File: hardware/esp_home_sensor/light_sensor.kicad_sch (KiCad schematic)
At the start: 3 parts

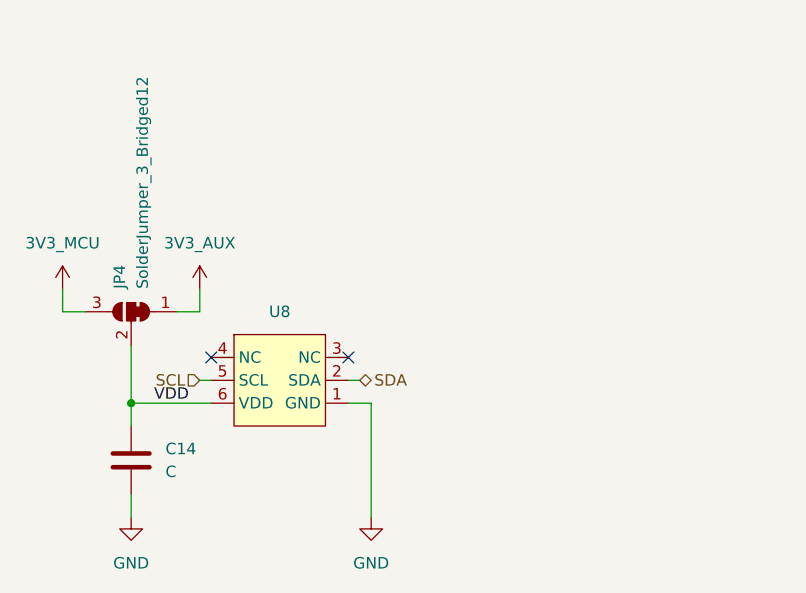
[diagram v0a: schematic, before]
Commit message: busses, display connector, footprint lib
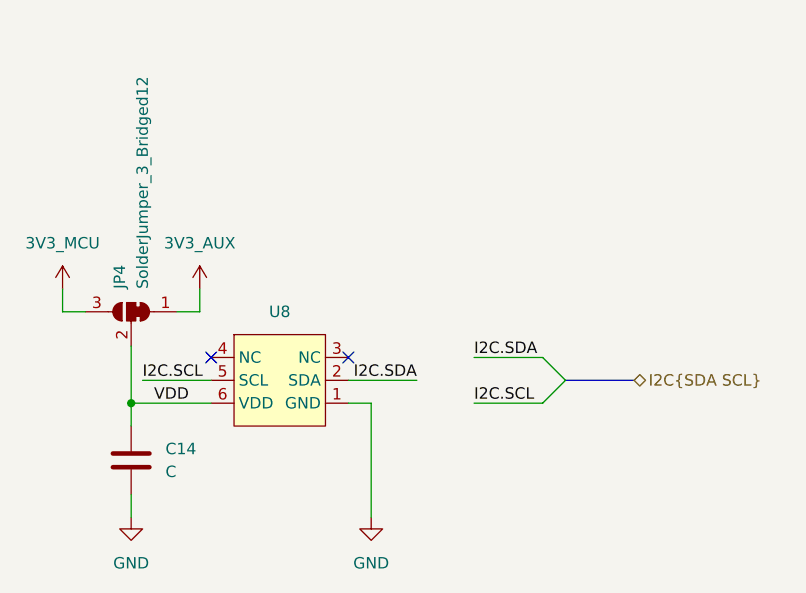
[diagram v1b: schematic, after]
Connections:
- net SCL renamed I2C.SCL
- net SDA renamed I2C.SDA
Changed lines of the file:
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@@
 		(at 135.89 97.79)
 	)
+	(bus_entry
+		(at 175.26 100.33)
+		(size -2.54 -2.54)
+		(stroke
+			(width 0)
+			(type default)
+		)
+	)
+	(bus_entry
+		(at 175.26 100.33)
+		(size -2.54 2.54)
+		(stroke
+			(width 0)
+			(type default)
+		)
+	)
+	(wire
+		(pts
+			(xy 165.1 102.87) (xy 172.72 102.87)
+		)
+		(stroke
+			(width 0)
+			(type default)
+		)
+	)
+	(wire
+		(pts
+			(xy 165.1 97.79) (xy 172.72 97.79)
+		)
+		(stroke
+			(width 0)
+			(type default)
+		)
+	)
 	(wire
 		(pts
@@
 	(wire
 		(pts
-			(xy 151.13 100.33) (xy 152.4 100.33)
+			(xy 151.13 100.33) (xy 158.75 100.33)
 		)
 		(stroke
@@
 	(wire
 		(pts
-			(xy 134.62 100.33) (xy 135.89 100.33)
-		)
-		(stroke
-			(width 0)
-			(type default)
-		)
-	)
-	(wire
-		(pts
 			(xy 153.67 102.87) (xy 151.13 102.87)
 		)
@@
 	(wire
 		(pts
+			(xy 128.27 100.33) (xy 135.89 100.33)
+		)
+		(stroke
+			(width 0)
+			(type default)
+		)
+	)
+	(wire
+		(pts
 			(xy 127 105.41) (xy 127 102.87)
 		)
@@
 		(pts
 			(xy 153.67 115.57) (xy 153.67 102.87)
+		)
+		(stroke
+			(width 0)
+			(type default)
+		)
+	)
+	(bus
+		(pts
+			(xy 175.26 100.33) (xy 182.88 100.33)
 		)
 		(stroke
@@
 		)
 	)
-	(hierarchical_label "SDA"
+	(label "I2C.SDA"
+		(at 158.75 100.33 180)
+		(effects
+			(font
+				(size 1.27 1.27)
+			)
+			(justify right bottom)
+		)
+	)
+	(label "I2C.SCL"
+		(at 165.1 102.87 0)
+		(effects
+			(font
+				(size 1.27 1.27)
+			)
+			(justify left bottom)
+		)
+	)
+	(label "I2C.SDA"
+		(at 165.1 97.79 0)
+		(effects
+			(font
+				(size 1.27 1.27)
+			)
+			(justify left bottom)
+		)
+	)
+	(label "I2C.SCL"
+		(at 128.27 100.33 0)
+		(effects
+			(font
+				(size 1.27 1.27)
+			)
+			(justify left bottom)
+		)
+	)
+	(hierarchical_label "I2C{SDA SCL}"
 		(shape bidirectional)
-		(at 152.4 100.33 0)
+		(at 182.88 100.33 0)
 		(effects
 			(font
@@
 		)
 	)
-	(hierarchical_label "SCL"
-		(shape input)
-		(at 134.62 100.33 180)
-		(effects
-			(font
-				(size 1.27 1.27)
-			)
-			(justify right)
-		)
-	)

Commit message: footprint assignment, buck
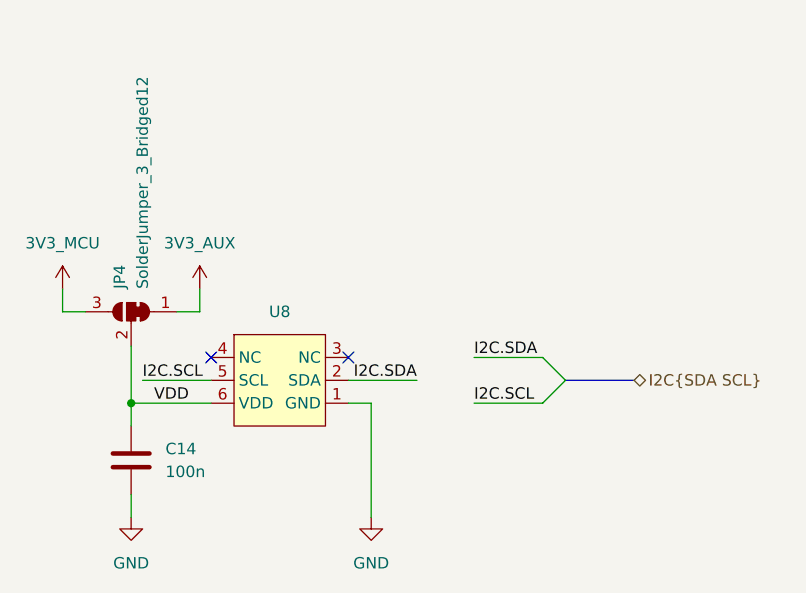
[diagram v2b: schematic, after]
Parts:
- C14: value C -> 100n; footprint (none) -> Capacitor_SMD:C_0402_1005Metric
- U8: Mfr. No. (none) -> VEML3235
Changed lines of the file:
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@@
 			)
 		)
-		(property "Value" "C"
+		(property "Value" "100n"
 			(at 130.81 110.4899 0)
 			(show_name no)
@@
 			)
 		)
-		(property "Footprint" ""
+		(property "Footprint" "Capacitor_SMD:C_0402_1005Metric"
 			(at 127.9652 113.03 0)
 			(hide yes)
@@
 		)
 		(property "Description" "Unpolarized capacitor"
+			(at 127 109.22 0)
+			(hide yes)
+			(show_name no)
+			(do_not_autoplace no)
+			(effects
+				(font
+					(size 1.27 1.27)
+				)
+			)
+		)
+		(property "Mfr. No." ""
 			(at 127 109.22 0)
 			(hide yes)
@@
 			)
 		)
+		(property "Mfr. No." ""
+			(at 127 92.71 90)
+			(hide yes)
+			(show_name no)
+			(do_not_autoplace no)
+			(effects
+				(font
+					(size 1.27 1.27)
+				)
+			)
+		)
 		(pin "3"
 		)
@@
 			(at 143.51 100.33 0)
 			(hide yes)
+			(show_name no)
+			(do_not_autoplace no)
+			(effects
+				(font
+					(size 1.27 1.27)
+				)
+			)
+		)
+		(property "Mfr. No." "VEML3235 "
+			(at 143.51 100.33 0)
+			(hide yes)

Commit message: minor update
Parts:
- JP4: footprint (none) -> Jumper:SolderJumper-3_P1.3mm_Bridged12_Pad1.0x1.5mm
- U8: value (none) -> VEML3235; footprint (none) -> esp_home_sensor:VEML3235
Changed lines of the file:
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@@
 			)
 		)
-		(property "Footprint" ""
+		(property "Footprint" "Jumper:SolderJumper-3_P1.3mm_Bridged12_Pad1.0x1.5mm"
 			(at 127 92.71 0)
 			(hide yes)
@@
 		(in_pos_files yes)
 		(dnp no)
-		(fields_autoplaced yes)
 		(property "Reference" "U8"
 			(at 143.51 92.71 0)
@@
 			)
 		)
-		(property "Value" ""
+		(property "Value" "VEML3235"
+			(at 143.51 94.234 0)
+			(show_name no)
+			(do_not_autoplace no)
+			(effects
+				(font
+					(size 1.27 1.27)
+				)
+			)
+		)
+		(property "Footprint" "esp_home_sensor:VEML3235"
 			(at 143.51 100.33 0)
-			(show_name no)
-			(do_not_autoplace no)
-			(effects
-				(font
-					(size 1.27 1.27)
-				)
-			)
-		)
-		(property "Footprint" ""
-			(at 143.51 100.33 0)
-			(hide yes)
+			(hide yes)

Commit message: layout
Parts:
- renumbered C14 to C16, JP4 to JP6
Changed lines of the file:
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@@
 		(in_pos_files yes)
 		(dnp no)
-		(property "Reference" "#PWR035"
+		(property "Reference" "#PWR053"
 			(at 153.67 121.92 0)
 			(hide yes)
@@
 			(project "esp_home_sensor"
 				(path "/1b1bee14-8d82-405b-b99d-415549a137e6/864cf49a-ab4e-430a-bc50-983d7167d916"
-					(reference "#PWR035")
+					(reference "#PWR053")
 					(unit 1)
 				)
@@
 		(dnp no)
 		(fields_autoplaced yes)
-		(property "Reference" "C14"
+		(property "Reference" "C16"
 			(at 130.81 107.9499 0)
 			(show_name no)
@@
 			(project "esp_home_sensor"
 				(path "/1b1bee14-8d82-405b-b99d-415549a137e6/864cf49a-ab4e-430a-bc50-983d7167d916"
-					(reference "C14")
+					(reference "C16")
 					(unit 1)
 				)
@@
 		(in_pos_files yes)
 		(dnp no)
-		(property "Reference" "JP4"
+		(property "Reference" "JP6"
 			(at 125.7299 90.17 90)
 			(show_name no)
@@
 			(project "esp_home_sensor"
 				(path "/1b1bee14-8d82-405b-b99d-415549a137e6/864cf49a-ab4e-430a-bc50-983d7167d916"
-					(reference "JP4")
+					(reference "JP6")
 					(unit 1)
 				)
@@
 		(in_pos_files yes)
 		(dnp no)
-		(property "Reference" "#PWR037"
+		(property "Reference" "#PWR051"
 			(at 127 121.92 0)
 			(hide yes)
@@
 			(project "esp_home_sensor"
 				(path "/1b1bee14-8d82-405b-b99d-415549a137e6/864cf49a-ab4e-430a-bc50-983d7167d916"
-					(reference "#PWR037")
+					(reference "#PWR051")
 					(unit 1)
 				)
@@
 		(dnp no)
 		(fields_autoplaced yes)
-		(property "Reference" "#PWR039"
+		(property "Reference" "#PWR050"
 			(at 119.38 93.98 0)
 			(hide yes)
@@
 			(project "esp_home_sensor"
 				(path "/1b1bee14-8d82-405b-b99d-415549a137e6/864cf49a-ab4e-430a-bc50-983d7167d916"
-					(reference "#PWR039")
+					(reference "#PWR050")
 					(unit 1)
 				)
@@
 		(dnp no)
 		(fields_autoplaced yes)
-		(property "Reference" "#PWR036"
+		(property "Reference" "#PWR052"
 			(at 134.62 93.98 0)
 			(hide yes)
@@
 			(project "esp_home_sensor"
 				(path "/1b1bee14-8d82-405b-b99d-415549a137e6/864cf49a-ab4e-430a-bc50-983d7167d916"
-					(reference "#PWR036")
-					(unit 1)
-				)
+					(reference "#PWR052")
+					(unit 1)
+				)

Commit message: in production
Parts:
- C16: Mfr. No. (none) -> GRM155R71H104KE14D
- U8: Mfr. No. VEML3235 -> VEML3235
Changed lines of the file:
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@@
 			)
 		)
-		(property "Mfr. No." ""
+		(property "Mfr. No." "GRM155R71H104KE14D"
 			(at 127 109.22 0)
 			(hide yes)
@@
 			)
 		)
-		(property "Mfr. No." "VEML3235 "
+		(property "Mfr. No." "VEML3235"
 			(at 143.51 100.33 0)
 			(hide yes)

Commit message: az
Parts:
- U8: Down_current (none) -> 1u; Supply_current (none) -> 250u
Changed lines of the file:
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@@
+			)
+		)
+		(property "Down_current" ""
+			(at 127 109.22 0)
+			(hide yes)
+			(show_name no)
+			(do_not_autoplace no)
+			(effects
+				(font
+					(size 1.27 1.27)
+				)
+			)
+		)
+		(property "Supply_current" ""
+			(at 127 109.22 0)
+			(hide yes)
+			(show_name no)
+			(do_not_autoplace no)
+			(effects
+				(font
+					(size 1.27 1.27)
+				)
 			)
 		)
@@
 			)
 		)
+		(property "Down_current" ""
+			(at 127 92.71 90)
+			(hide yes)
+			(show_name no)
+			(do_not_autoplace no)
+			(effects
+				(font
+					(size 1.27 1.27)
+				)
+			)
+		)
+		(property "Supply_current" ""
+			(at 127 92.71 90)
+			(hide yes)
+			(show_name no)
+			(do_not_autoplace no)
+			(effects
+				(font
+					(size 1.27 1.27)
+				)
+			)
+		)
 		(pin "3"
 		)
@@
 			)
 		)
-		(property "Datasheet" ""
+		(property "Datasheet" "https://www.vishay.com/docs/80131/veml3235.pdf"
 			(at 143.51 100.33 0)
 			(hide yes)
@@
 			(at 143.51 100.33 0)
 			(hide yes)
+			(show_name no)
+			(do_not_autoplace no)
+			(effects
+				(font
+					(size 1.27 1.27)
+				)
+			)
+		)
+		(property "Down_current" "1u"
+			(at 143.51 100.33 0)
+			(hide yes)
+			(show_name no)
+			(do_not_autoplace no)
+			(effects
+				(font
+					(size 1.27 1.27)
+				)
+			)
+		)
+		(property "Supply_current" "250u"
+			(at 143.51 100.33 0)
+			(hide yes)
